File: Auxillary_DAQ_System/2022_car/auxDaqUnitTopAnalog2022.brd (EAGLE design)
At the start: 38.1 x 193 mm, 30 parts

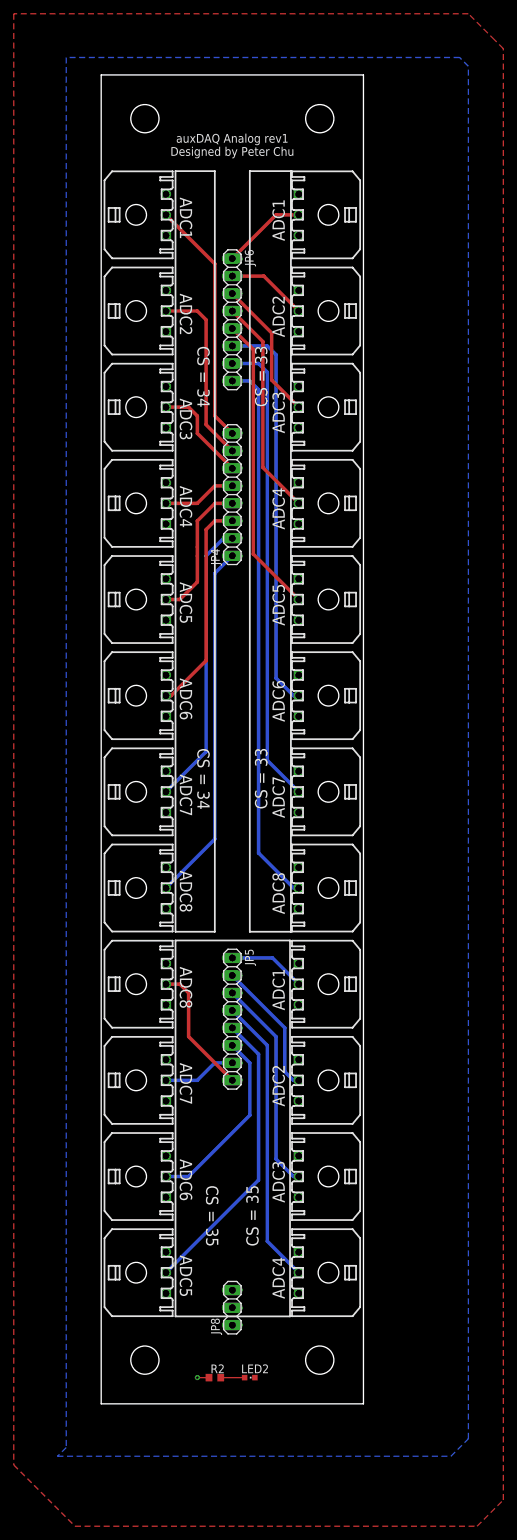
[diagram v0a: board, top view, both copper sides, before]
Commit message: Bottom board has some airwires, but everything should line up
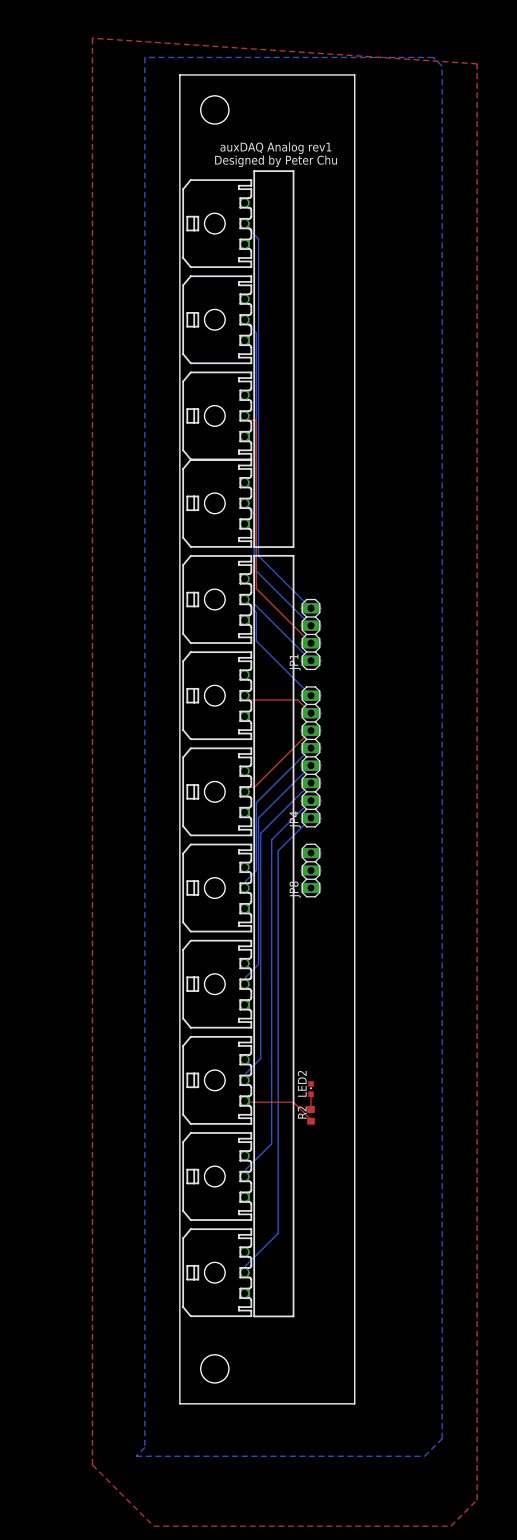
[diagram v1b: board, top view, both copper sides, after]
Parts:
- removed A0, A1, A10, A11, A2, A3, A4, A5, A6, A7, A8, A9: (no value), GTOR - Microfit Connector:43650-0300
- removed JP5, JP6: (no value), GTOR - Connectors:1X08
- added JP1: (no value), GTOR - Connectors:1X04
- moved A12 112.3 mm to (16.5, 130.8)
- moved A13 111.1 mm to (16.5, 143.5)
- moved A14 111.1 mm to (16.5, 157.5)
- moved A15 111.1 mm to (16.5, 171.4)
- moved JP8 64.5 mm to (30.5, 77.5)
- moved A16 57.0 mm to (16.5, 19.1)
- moved A17 57.0 mm to (16.5, 33.0)
- moved A18 57.0 mm to (16.5, 47.0)
- moved A19 57.0 mm to (16.5, 61.0)
- moved A20 57.0 mm to (16.5, 74.9)
- moved A21 57.0 mm to (16.5, 88.9)
- moved A22 57.0 mm to (16.5, 102.9)
- moved A23 57.0 mm to (16.5, 116.8)
- moved LED2 42.8 mm to (30.5, 45.7), turned to 0 degrees
- moved R2 40.6 mm to (30.5, 41.9), turned to 90 degrees
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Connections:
- removed net ADC1: A0.P$2, JP6.1
- removed net ADC10: A9.P$2, JP5.2
- removed net ADC11: A10.P$2, JP5.3
- removed net ADC12: A11.P$2, JP5.4
- removed net ADC2: A1.P$2, JP6.2
- removed net ADC3: A2.P$2, JP6.3
- removed net ADC4: A3.P$2, JP6.4
- removed net ADC5: A4.P$2, JP6.5
- removed net ADC6: A5.P$2, JP6.6
- removed net ADC7: A6.P$2, JP6.7
- removed net ADC8: A7.P$2, JP6.8
- removed net ADC9: A8.P$2, JP5.1
- net +5V: no longer A0.P$1, A1.P$1, A10.P$1, A11.P$1, A2.P$1, A3.P$1, A4.P$1, A5.P$1, A6.P$1, A7.P$1, A8.P$1, A9.P$1
- net ADC13: now also JP1.1; no longer JP5.5
- net ADC14: now also JP1.2; no longer JP5.6
- net ADC15: now also JP1.3; no longer JP5.7
- net ADC16: now also JP1.4; no longer JP5.8
- net GND: no longer A0.P$3, A1.P$3, A10.P$3, A11.P$3, A2.P$3, A3.P$3, A4.P$3, A5.P$3, A6.P$3, A7.P$3, A8.P$3, A9.P$3
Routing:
- net ADC8: track 79.6 -> 0.00 mm
- net ADC7: track 68.5 -> 0.00 mm
- net ADC6: track 58.2 -> 0.00 mm
- net ADC5: track 43.4 -> 0.00 mm
- net ADC12: track 42.1 -> 0.00 mm
- net ADC16: track 19.2 -> 60.0 mm
- net ADC15: track 10.7 -> 48.5 mm
- net ADC4: track 31.9 -> 0.00 mm
- net ADC11: track 31.6 -> 0.00 mm
- net ADC3: track 20.5 -> 0.00 mm
- net ADC10: track 19.7 -> 0.00 mm
- net ADC17: track 52.3 -> 70.1 mm
- net ADC24: track 35.7 -> 18.0 mm
- net ADC18: track 41.6 -> 58.7 mm
- net ADC23: track 27.0 -> 10.7 mm
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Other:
- board size 38.1 x 193 mm -> 25.4 x 193 mm
- board text removed: "ADC1"
- board text removed: "ADC2"
- board text removed: "ADC3"
- board text removed: "ADC4"
- board text removed: "ADC5"
- board text removed: "ADC6"
- board text removed: "ADC7"
- board text removed: "ADC8"
- board text removed: "CS = 33"
- board text removed: "CS = 34"
- board text removed: "CS = 35"

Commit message: Mostly done with Aux Daq Rework
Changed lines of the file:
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@@
 <wire x1="36.83" y1="193.04" x2="11.43" y2="193.04" width="0" layer="20"/>
 <wire x1="11.43" y1="193.04" x2="11.43" y2="0" width="0" layer="20"/>
-<hole x="16.51" y="187.96" drill="4.1"/>
-<hole x="16.51" y="5.08" drill="4.1"/>
+<hole x="16.51" y="187.96" drill="3.3"/>
+<hole x="16.51" y="5.08" drill="3.3"/>
 <text x="25.4" y="181.61" size="1.27" layer="25" rot="SR0" align="center">auxDAQ Analog rev1
 Designed by Peter Chu</text>
